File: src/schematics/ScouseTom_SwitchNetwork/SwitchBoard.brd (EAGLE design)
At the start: 160 x 100 mm, 47 parts, among them U1 ADUM1410ARWZ, U2 MCP73831, X1 DSUB _T, X2 DSUB_B, X3 USB-MICROB

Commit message: Added Mak Connector for Silicon Elec to Schematics. Started routing Switchboard
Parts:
- added C11, C12, C13, C14, C15, C18, C5, C6, C7, C8: 0.1uF, resistor:C0805
- added DSUB3: CTR_IN, con-subd:F09HP
- added JP3, JP4: (no value), pinhead:1X02
- added JP5: (no value), pinhead:2X09
- DSUB1: value (none) -> CTR_OUT
- DSUB2: value CTR_DSUB -> CTR_ARD
- moved R9 358.8 mm to (148.0, 84.5), flipped to the bottom, turned to 90 degrees
- moved NSW5 343.0 mm to (138.4, 85.1), flipped to the bottom, turned to 90 degrees
- moved C9 331.7 mm to (-66.0, 91.4), turned to 270 degrees
- moved R14 330.1 mm to (-73.7, 90.2), turned to 180 degrees
- moved D4 327.6 mm to (-73.7, 88.9), turned to 90 degrees
- moved U2 326.9 mm to (-68.6, 88.9), turned to 0 degrees
- moved R13 325.1 mm to (-73.7, 87.6), turned to 180 degrees
- moved C10 319.3 mm to (-68.6, 85.1), turned to 180 degrees
- moved JP2 319.0 mm to (-53.3, 85.1), turned to 270 degrees
- moved JP9 317.2 mm to (-72.4, 83.8), turned to 270 degrees
- moved JP12 316.2 mm to (-58.4, 83.8), turned to 90 degrees
- moved X3 315.8 mm to (-77.5, 82.5), turned to 270 degrees
- moved NSW4 309.0 mm to (137.8, 59.1), flipped to the bottom, turned to 90 degrees
- moved R8 289.5 mm to (140.3, 47.6), flipped to the bottom, turned to 90 degrees
- moved R5 280.2 mm to (130.8, 85.1)
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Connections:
- new net DIN+_DCHN: DSUB3.3, JP5.10
- new net DIN-_DCHN: DSUB3.7, JP5.8
- new net GND_DCHN: DSUB3.6, JP5.4
- new net N$10: DSUB1.G1, DSUB1.G2, JP3.2
- new net N$12: DSUB3.G1, DSUB3.G2, JP4.1
- new net RESET: DSUB1.8, JP5.11
- new net RESET_DCHN: DSUB3.8, JP5.12
- new net SCLK_DCHN: DSUB3.2, JP5.6
- new net SYNC: DSUB1.4, JP5.13
- new net SYNC_DCHN: DSUB3.4, JP5.14
- new net TEST_1_DCHN: DSUB3.5, JP5.18
- new net TEST_2_DCHN: DSUB3.1, JP5.2
- new net VDD_DCHN: DSUB3.9, JP5.16
- net AGND: now also C11.1, C12.1, C13.1, C14.1, C15.1, C18.1, C5.1, C6.1, C7.1, C8.1, DSUB1.6, JP3.1, JP4.2, JP5.3
- net DIN+: now also DSUB1.3, JP5.9
- net DIN-: now also DSUB1.7, JP5.7
- net SCLK: now also DSUB1.2, JP5.5
- net TEST_1: now also DSUB1.5, JP5.17
- net TEST_2: now also DSUB1.1, JP5.1
- net VDD: now also C11.2, C12.2, C13.2, C14.2, C15.2, C18.2, C5.2, C6.2, C7.2, C8.2, DSUB1.9, JP5.15
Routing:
- net OUT_16: track 0.00 -> 141.0 mm, vias 0 -> 1
- net OUT_15: track 0.00 -> 139.5 mm, vias 0 -> 1
- net OUT_14: track 0.00 -> 138.0 mm, vias 0 -> 1
- net OUT_13: track 0.00 -> 136.6 mm, vias 0 -> 1
- net OUT_12: track 0.00 -> 135.1 mm, vias 0 -> 1
- net OUT_11: track 0.00 -> 133.6 mm, vias 0 -> 1
- net OUT_10: track 0.00 -> 132.1 mm, vias 0 -> 1
- net OUT_9: track 0.00 -> 130.6 mm, vias 0 -> 1
- net OUT_8: track 0.00 -> 103.1 mm, vias 0 -> 1
- net OUT_7: track 0.00 -> 101.6 mm, vias 0 -> 1
- net OUT_6: track 0.00 -> 100.1 mm, vias 0 -> 1
- net OUT_5: track 0.00 -> 98.6 mm, vias 0 -> 1
- net OUT_4: track 0.00 -> 97.1 mm, vias 0 -> 1
- net OUT_3: track 0.00 -> 95.6 mm, vias 0 -> 1
- net OUT_2: track 0.00 -> 94.1 mm, vias 0 -> 1
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
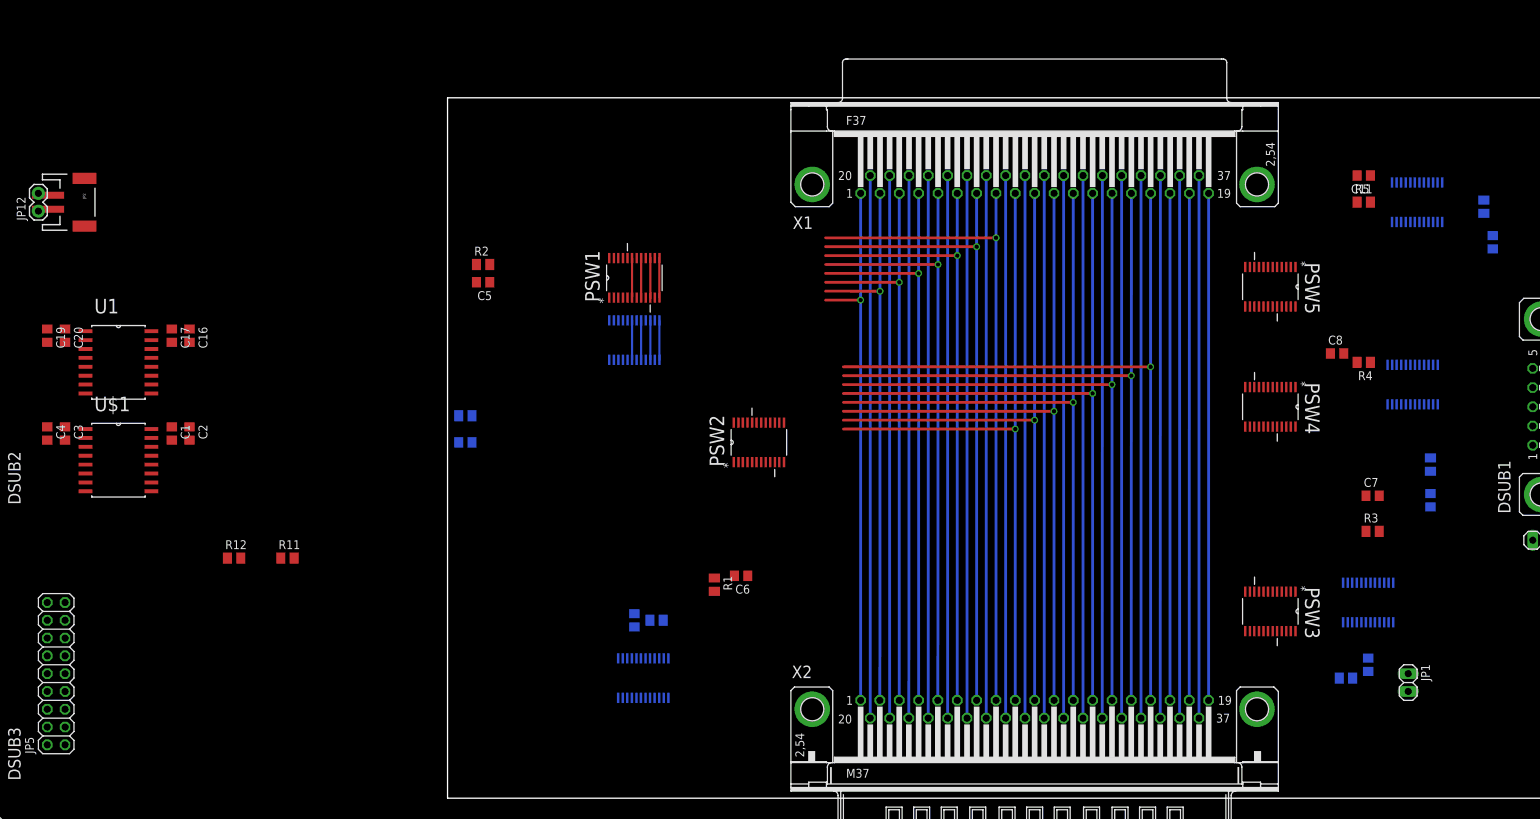
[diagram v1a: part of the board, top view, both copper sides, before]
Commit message: SwNet - left hand side layout done
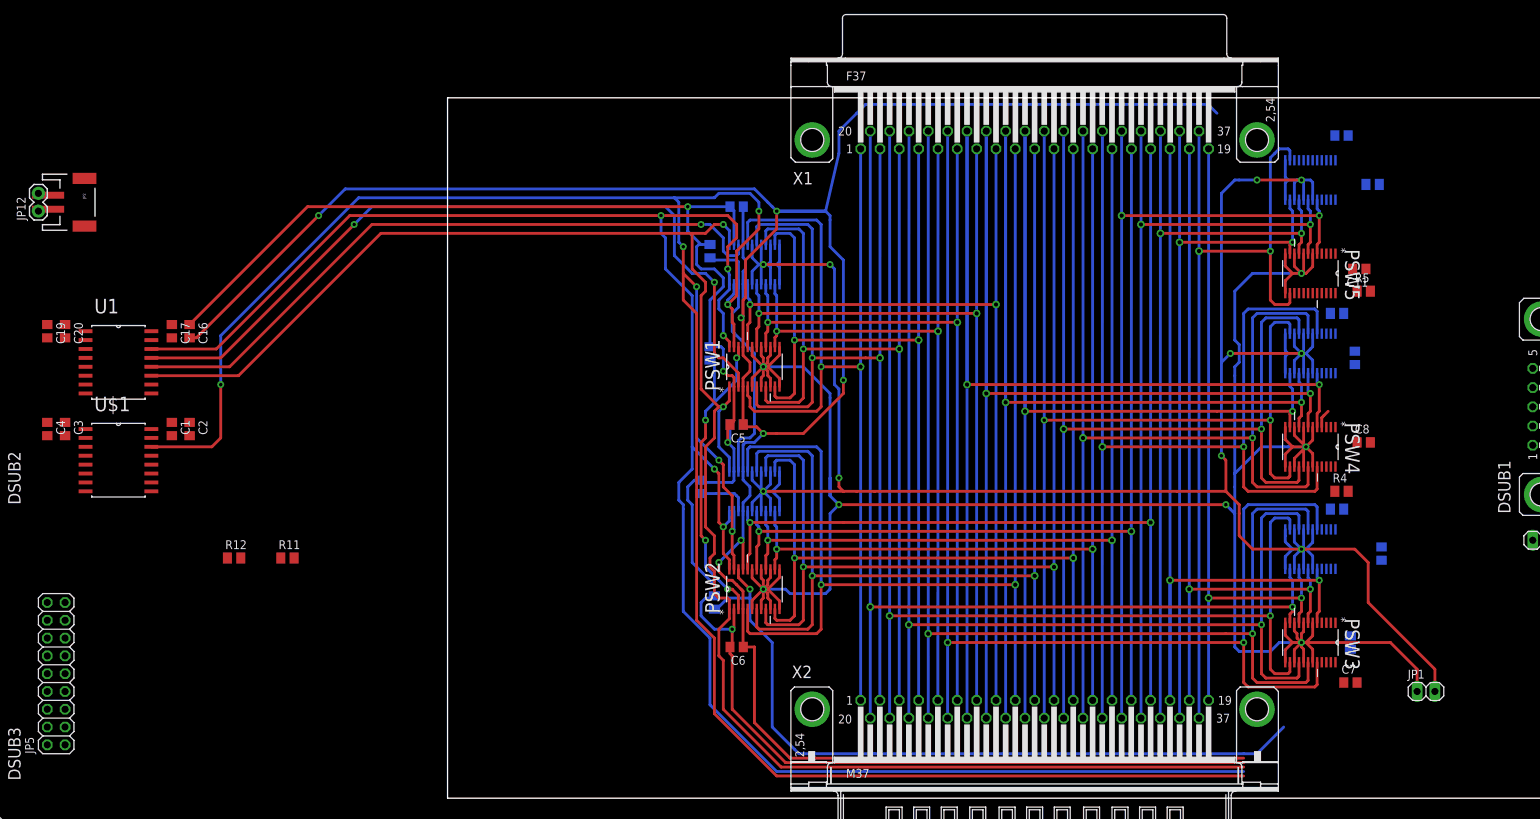
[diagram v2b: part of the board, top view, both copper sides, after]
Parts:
- moved R10 133.7 mm to (132.1, 87.6)
- moved R7 96.0 mm to (36.2, 44.4), turned to 90 degrees
- moved R2 58.5 mm to (38.1, 27.9), flipped to the bottom, turned to 90 degrees
- moved R6 53.3 mm to (37.5, 78.1), turned to 90 degrees
- moved C12 51.3 mm to (41.3, 84.5)
- moved C5 41.5 mm to (41.3, 53.3)
- moved R1 33.0 mm to (37.5, 63.5), flipped to the bottom, turned to 90 degrees
- moved C13 31.5 mm to (41.3, 53.3), turned to 0 degrees
- moved NSW2 31.0 mm to (43.8, 43.8)
- moved C7 26.9 mm to (128.9, 16.5)
- moved C18 26.4 mm to (127.6, 94.6), turned to 180 degrees
- moved R9 25.9 mm to (127.0, 69.2), turned to 180 degrees
- moved C15 23.0 mm to (129.5, 62.9)
- moved PSW1 21.3 mm to (43.8, 61.6)
- moved PSW2 21.0 mm to (43.8, 29.8)
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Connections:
- net N$1 renamed DIN+2
- net N$2 renamed DIN+4
- net N$3 renamed DIN+3
- net N$4 renamed DIN-2
- net N$5 renamed DIN+5
- net N$6 renamed DIN-3
- net N$7 renamed DIN-4
- net N$8 renamed DIN-5
- removed net RESET: DSUB1.8, JP5.11
- removed net SYNC: DSUB1.4, JP5.13
- net DIN+: no longer DSUB1.3
- net DIN-: no longer DSUB1.7
- net DOUT+: now also DSUB1.3
- net DOUT-: now also DSUB1.7
- net ~RESET: now also DSUB1.8, JP5.11
- net ~SYNC: now also DSUB1.4, JP5.13
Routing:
- net AGND: track 0.00 -> 397.5 mm, vias 0 -> 7
- net ~RESET: track 0.00 -> 340.5 mm, vias 0 -> 7
- net IN-: track 22.6 -> 353.0 mm, vias 0 -> 10
- net IN+: track 22.6 -> 341.7 mm, vias 0 -> 7
- net ~SYNC: track 0.00 -> 288.1 mm, vias 0 -> 5
- net VDD: track 0.00 -> 266.2 mm, vias 0 -> 4
- net SCLK: track 0.00 -> 260.0 mm, vias 0 -> 2
- net OUT_32: track 77.5 -> 202.0 mm, vias 0 -> 2
- net OUT_31: track 77.5 -> 197.1 mm, vias 0 -> 2
- net OUT_30: track 77.5 -> 192.3 mm, vias 0 -> 2
- net DIN+: track 0.00 -> 113.8 mm, vias 0 -> 2
- net OUT_24: track 77.5 -> 189.8 mm, vias 0 -> 2
- net OUT_23: track 77.5 -> 187.5 mm, vias 0 -> 2
- net OUT_29: track 77.5 -> 187.4 mm, vias 0 -> 2
- net OUT_22: track 77.5 -> 185.2 mm, vias 0 -> 2
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
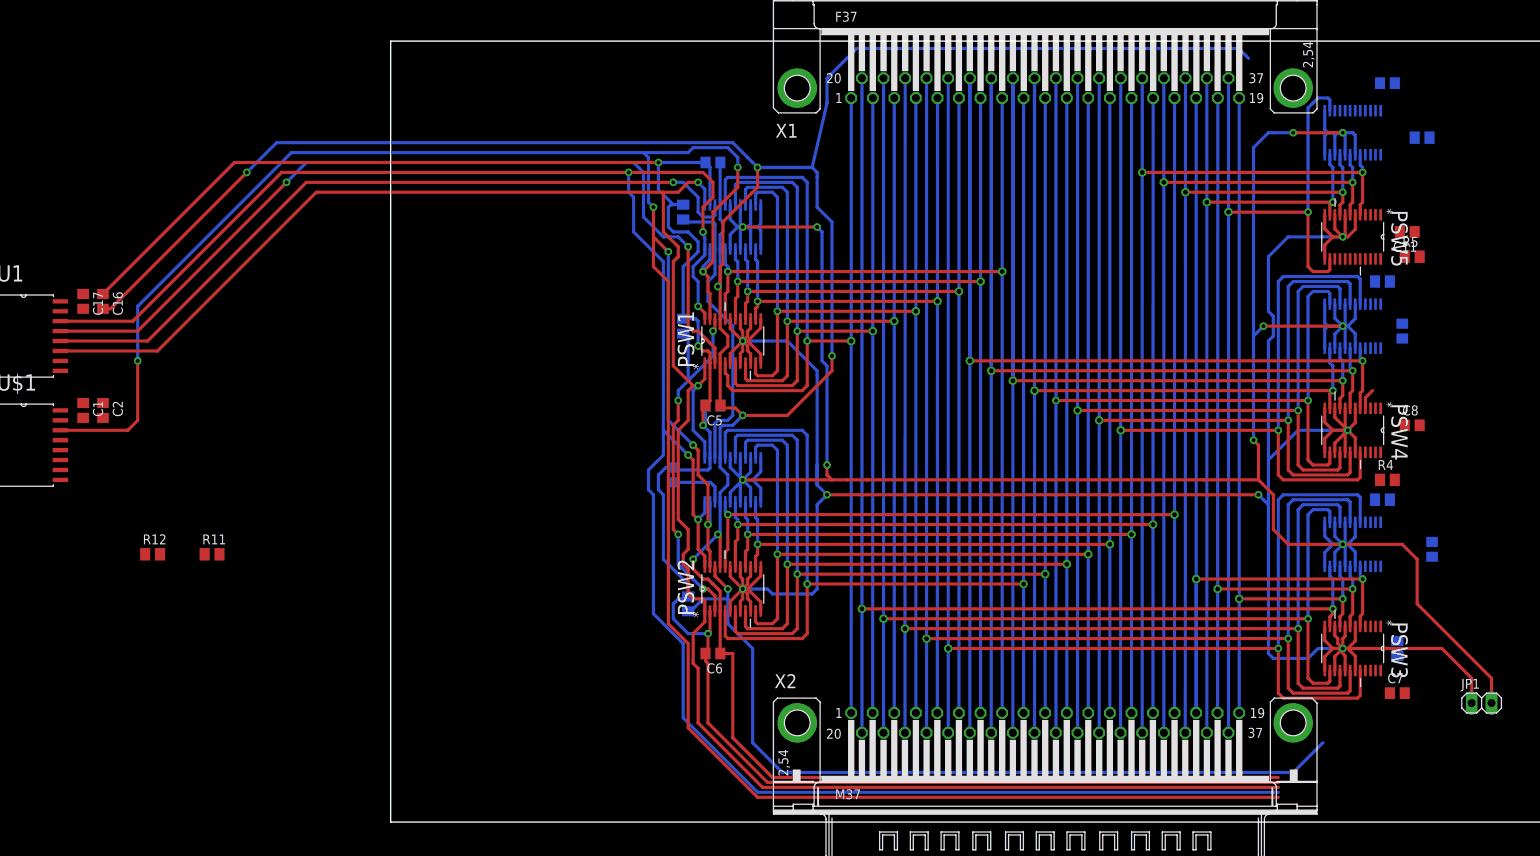
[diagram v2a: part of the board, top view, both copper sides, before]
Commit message: SwitchBoard Switches routed
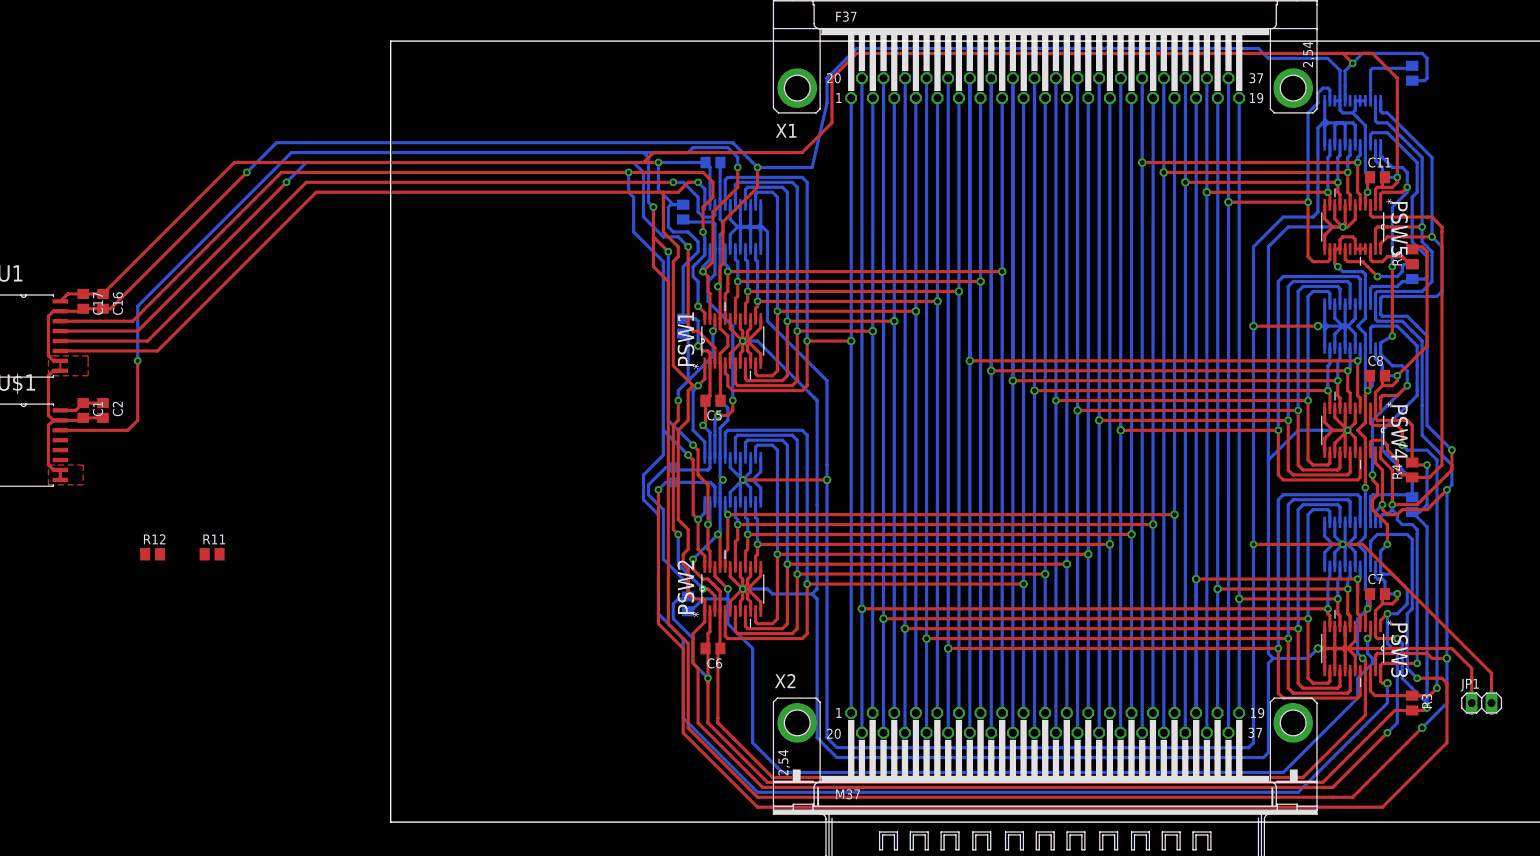
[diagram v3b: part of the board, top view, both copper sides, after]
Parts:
- moved C7 13.0 mm to (126.4, 29.2)
- moved C18 12.1 mm to (126.4, 82.6)
- moved C14 9.02 mm to (126.4, 29.2), turned to 180 degrees
- moved R10 8.35 mm to (130.8, 95.9), turned to 270 degrees
- moved C11 7.96 mm to (126.4, 82.5), turned to 0 degrees
- moved C8 7.75 mm to (126.4, 57.1)
- moved R3 7.24 mm to (130.8, 15.2), flipped to the top, turned to 270 degrees
- moved C15 6.54 mm to (126.4, 57.2), turned to 180 degrees
- moved R9 4.02 mm to (130.8, 70.5), turned to 90 degrees
- moved R8 3.86 mm to (130.8, 40.6), turned to 270 degrees
- moved R4 3.42 mm to (130.8, 45.1), turned to 90 degrees
- moved NSW5 1.27 mm to (123.2, 89.5)
- moved PSW5 1.27 mm to (123.2, 76.2)
- moved C13 0.63 mm to (41.3, 54.0)
- moved C5 0.63 mm to (41.3, 54.0)
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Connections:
- removed net EX+_1D: PSW5.15
- removed net EX+_1S: PSW5.16
- removed net EX+_3D: PSW5.19
- removed net EX+_3S: PSW5.20
- removed net EX-_1D: NSW5.15
- removed net EX-_1S: NSW5.16
- removed net EX-_3D: NSW5.19
- removed net EX-_3S: NSW5.20
- net AGND: now also NSW5.15, NSW5.16, NSW5.19, NSW5.20, PSW5.15, PSW5.16, PSW5.19, PSW5.20
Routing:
- net VDD: track 266.2 -> 581.2 mm, vias 4 -> 12
- net DIN-3: track 7.50 -> 186.8 mm, vias 0 -> 2
- net ~RESET: track 340.5 -> 500.7 mm, vias 7 -> 12
- net ~SYNC: track 288.1 -> 431.6 mm, vias 5 -> 10
- net AGND: track 397.5 -> 517.1 mm, vias 7 -> 12
- net SCLK: track 260.0 -> 379.2 mm, vias 2 -> 10
- net DIN+5: track 0.00 -> 56.3 mm
- net DIN+4: track 0.00 -> 54.5 mm, vias 0 -> 2
- net IN-: track 353.0 -> 402.5 mm, vias 10 -> 6
- net DIN-4: track 0.00 -> 41.3 mm
- net DIN-5: track 0.00 -> 34.5 mm
- net IN+: track 341.7 -> 371.3 mm, vias 7 -> 5
- net DIN+3: track 106.4 -> 123.6 mm, vias 1 -> 2
- net DOUT-: track 0.00 -> 9.48 mm
- net DOUT+: track 0.00 -> 7.92 mm
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- added copper zone on layer 1, net AGND

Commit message: Switch Board Layout finished, needs text and logo
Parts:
- removed D4: red, SparkFun:LED-0603
- added C21, C24, C25: 10uF, resistor:C0805
- added C22, C26: 100uF, rcl:CT6032
- added C23: 0.01uF, resistor:C0805
- added C28: 2.2uF, resistor:C0805
- added CHRG: YELLOW, led:SML0805
- added FULL, LBO, PWR: GREEN, led:SML0805
- added IC2: LT1763CDE-5, linear-technology:DFN12
- added L2: 6.8uH, WE-PD:WE-PD_7332/7345_PLASTIC_BASE
- added ON/OFF: (no value), pinhead:1X02
- added R15: 2k, rcl:M0805
- added R16: 1.8M, rcl:M0805
- added R17, R21: 1k, rcl:M0805
- added R18: 200k, rcl:M0805
- added R19: 82k, rcl:M0805
- added R20: 2M, rcl:M0805
- added R22: 4.7k, rcl:M0805
- added R23: 360k, rcl:M0805
- added R24: 47k, rcl:M0805
- added T1: (no value), transistor:SOT23-BEC
- added U3: TPS61090RSAR, Adafruit PowerBoost 500C:QFN16-4X4
- C10: value 4.7uF -> 10uF; device SparkFun:0402-CAP -> resistor:C0805
- C9: value 4.7uF -> 0.1uF; device SparkFun:0402-CAP -> resistor:C0805
- R13: value 470 -> 1k; device SparkFun:0402-RES -> rcl:M0805
- R14: value 2k -> 470; device SparkFun:0402-RES -> rcl:M0805
- moved JP5 87.6 mm to (26.0, 48.9), turned to 270 degrees
- moved JP1 83.1 mm to (149.2, 97.8), turned to 270 degrees
- moved JP4 70.7 mm to (-5.71, 33.0)
- moved C9 70.1 mm to (3.81, 85.7)
- moved R14 61.8 mm to (-13.3, 76.8)
- moved R13 61.8 mm to (-13.3, 74.3)
- moved U2 60.6 mm to (-8.26, 83.2), turned to 90 degrees
- moved X3 58.4 mm to (-19.0, 83.2)
- moved JP9 58.4 mm to (-14.0, 84.5)
- moved C10 57.2 mm to (-11.4, 83.2), turned to 270 degrees
- moved DSUB3 54.7 mm to (-12.7, 20.3)
- moved DSUB2 54.6 mm to (-12.7, 55.2)
- moved C20 54.0 mm to (-0.64, 66.7)
- moved C1 54.0 mm to (14.6, 52.7)
- moved C17 54.0 mm to (14.6, 66.7)
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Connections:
- removed net N$14: R13.1, U2.1
- removed net N$17: JP12.2, JP2.1
- removed net VBATT: C10.1, JP12.1, JP2.2, U2.3
- new net LBO: R22.1, U3.12
- new net LB_REF: R20.1, R23.2, U3.9
- new net N$2: CHRG.C, R14.2
- new net N$3: C23.1, IC2.3, IC2.5
- new net N$4: C23.2, IC2.6
- new net N$5: FULL.A, R13.2
- new net N$6: R16.1, R19.2
- new net N$7: PWR.C, R17.1
- new net N$8: R21.1, T1.C
- new net PROG: R15.2, U2.5
- new net STAT: R13.1, R14.1, U2.1
- new net SW: L2.2, U3.3, U3.4
- new net VBATT_A: C24.1, JP12.1, JP2.2, ON/OFF.1, U2.3
- new net VBATT_B: C25.1, C9.1, L2.1, ON/OFF.2, R20.2, R24.2, T1.E, U3.11, U3.8
- new net VREG: C21.1, C26.+, C28.1, IC2.10, IC2.11, IC2.8, PWR.A, R16.2, U3.1, U3.15, U3.16
- new net VSET: R18.2, R19.1, U3.14
- net 5VIN: now also C10.1, CHRG.A; no longer C9.1, D4.A
- net AGND: now also C21.2, C22.-, C24.2, C25.2, C26.-, C28.2, FULL.C, IC2.7, IC2.EXP, JP12.2, JP2.1, LBO.C, R15.1, R17.2, R18.1, R23.1, U3.10, U3.13, U3.5, U3.6, U3.7, U3.EXP; no longer R14.2
- net DIN+: now also JP5.7; no longer JP5.9
- net DIN+_DCHN: now also JP5.8; no longer JP5.10
- net DIN-: now also JP5.9; no longer JP5.7
- net DIN-_DCHN: now also JP5.10; no longer JP5.8
- net GND: now also U$1.2, U$1.8
- net N$11: now also R22.2, R24.1, T1.B; no longer R14.1, U2.5
- net N$9: now also LBO.A, R21.2; no longer D4.C, R13.2
- net RESET_DCHN: now also JP5.14; no longer JP5.12
- net SCLK: now also JP5.11; no longer JP5.5
- net SCLK_DCHN: now also JP5.12; no longer JP5.6
- net SYNC_DCHN: now also JP5.6; no longer JP5.14
- net TEST_1: now also JP5.15; no longer JP5.17
- net TEST_1_DCHN: now also JP5.16; no longer JP5.18
- net TEST_2: now also JP5.17; no longer JP5.1
- net TEST_2_DCHN: now also JP5.18; no longer JP5.2
- net VDD: now also C22.+, IC2.2, JP5.1; no longer JP5.15
- net VDD_DCHN: now also JP5.2; no longer JP5.16
- net ~RESET: now also JP5.13; no longer JP5.11
- net ~SYNC: now also JP5.5; no longer JP5.13
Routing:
- net TEST_2: track 0.00 -> 312.4 mm, vias 0 -> 6
- net TEST_1: track 0.00 -> 261.1 mm, vias 0 -> 2
- net AGND: track 517.1 -> 668.2 mm, vias 12 -> 34
- net IN+: track 371.3 -> 511.5 mm
- net IN-: track 402.5 -> 512.2 mm, vias 6 -> 10
- net GND_DCHN: track 0.00 -> 80.7 mm
- net VDD_DCHN: track 0.00 -> 74.1 mm
- net VDD: track 581.2 -> 509.0 mm, vias 12 -> 15
- net DIN+_DCHN: track 0.00 -> 71.8 mm, vias 0 -> 1
- net SYNC_DCHN: track 0.00 -> 71.2 mm, vias 0 -> 1
- net DIN-_DCHN: track 0.00 -> 68.3 mm, vias 0 -> 1
- net TEST_2_DCHN: track 0.00 -> 66.1 mm
- net SCLK_DCHN: track 0.00 -> 63.6 mm
- net DIN+: track 113.8 -> 55.9 mm, vias 2 -> 3
- net RESET_DCHN: track 0.00 -> 57.1 mm
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- added copper zone on layer 16, net AGND
- added copper zone on layer 1, net GND
- added copper zone on layer 16, net GND
- added copper zone on layer 1, net IN+
- added copper zone on layer 16, net IN-
- added copper zone on layer 1, net N$3
- added copper zone on layer 1, net SW
- added copper zone on layer 1, net VBATT_A
- added copper zone on layer 1, net VBATT_B
- added copper zone on layer 1, net VDD
- added copper zone on layer 1, net VREG
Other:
- board size 160 x 100 mm -> 172.7 x 97.5 mm
